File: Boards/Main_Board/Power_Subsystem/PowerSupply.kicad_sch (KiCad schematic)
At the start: 26 parts, among them IC4 LM2576HVS-5.0_NOPB, J10 KLDHCX-8-0202-A, U10 LM2576SX-3.3-NOPB

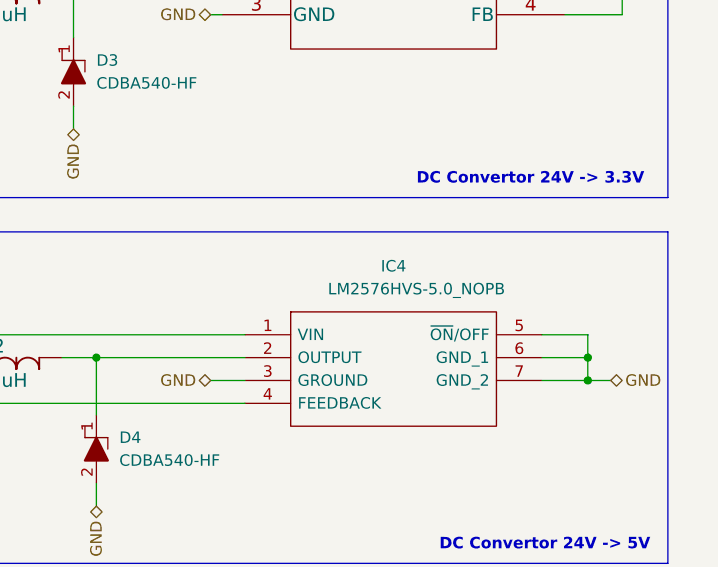
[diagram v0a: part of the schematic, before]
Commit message: Correct spacing on sensor board, refactor datasheets and project libraries
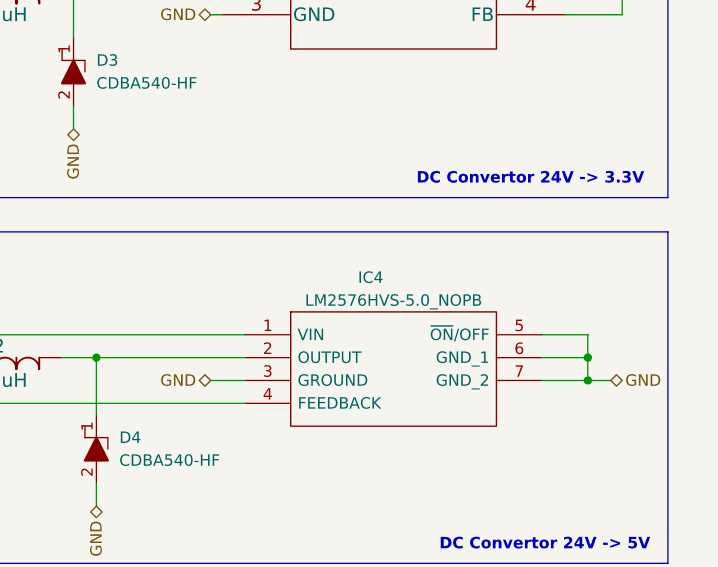
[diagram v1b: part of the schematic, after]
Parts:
- C25, C26: symbol CL10B104KB8NNC:CL10B104KB8NNNC -> CL10B104KB8NNNC:CL10B104KB8NNNC
- IC4: symbol LM25766HVS-5.0_NOPB:LM2576HVS-5.0_NOPB -> LM2576HVS-5.0_NOPB:LM2576HVS-5.0_NOPB
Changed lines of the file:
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@@
     (pin "2")
   )
-  (symbol (lib_id "CL10B104KB8NNC:CL10B104KB8NNNC") (at 123.19 148.59 90) (unit 1)
+  (symbol (lib_id "CL10B104KB8NNNC:CL10B104KB8NNNC") (at 123.19 148.59 90) (unit 1)
     (in_bom yes) (on_board yes)
     (property "Reference" "C26" (id 0) (at 118.11 146.05 90)
@@
     (pin "4")
   )
-  (symbol (lib_id "LM25766HVS-5.0_NOPB:LM2576HVS-5.0_NOPB") (at 184.15 133.35 0) (unit 1)
-    (in_bom yes) (on_board yes)
-    (property "Reference" "IC4" (id 0) (at 200.66 125.73 0))
-    (property "Value" "LM2576HVS-5.0_NOPB" (id 1) (at 203.2 128.27 0))
+  (symbol (lib_id "LM2576HVS-5.0_NOPB:LM2576HVS-5.0_NOPB") (at 184.15 133.35 0) (unit 1)
+    (in_bom yes) (on_board yes)
+    (property "Reference" "IC4" (id 0) (at 198.12 127 0))
+    (property "Value" "LM2576HVS-5.0_NOPB" (id 1) (at 200.66 129.54 0))
     (property "Footprint" "LM2576HVS50NOPB" (id 2) (at 218.44 130.81 0)
       (effects (font (size 1.27 1.27)) (justify left) hide)
@@
       (effects (font (size 1.27 1.27)) (justify left) hide)
     )
-    (property "Manufacturer's Part Number" "LM2576HVS-5.0/NOPB" (id 10) (at 184.15 133.35 0)
-      (effects (font (size 1.27 1.27)) hide)
+    (property "Manufacturer's Part Number" "LM2576HVS-5.0/NOPB" (id 10) (at 218.44 148.59 0)
+      (effects (font (size 1.27 1.27)) (justify left) hide)
     )
     (property "Digikey Part Number" "LM2576HVS-5.0/NOPB-ND" (id 11) (at 218.44 143.51 0)
@@
       (effects (font (size 1.27 1.27)) (justify left) hide)
     )
-    (property "Mouser Link" "https://www.mouser.com/ProductDetail/Texas-Instruments/LM2576HVS-5.0-NOPB?qs=X1J7HmVL2ZHJEgTkAH3ZCg%3D%3D" (id 8) (at 184.15 133.35 0)
+    (property "Mouser Link" "https://www.mouser.com/ProductDetail/Texas-Instruments/LM2576HVS-5.0-NOPB?qs=X1J7HmVL2ZHJEgTkAH3ZCg%3D%3D" (id 8) (at 196.85 123.19 0)
       (effects (font (size 1.27 1.27)) hide)
     )
@@
     (pin "")
   )
-  (symbol (lib_id "CL10B104KB8NNC:CL10B104KB8NNNC") (at 123.19 106.68 90) (unit 1)
+  (symbol (lib_id "CL10B104KB8NNNC:CL10B104KB8NNNC") (at 123.19 106.68 90) (unit 1)
     (in_bom yes) (on_board yes)
     (property "Reference" "C25" (id 0) (at 119.38 104.14 90)
@@
     (pin "2")
   )
-  (symbol (lib_id "860020573008:860020573008860020573008") (at 127 104.14 90) (mirror x) (unit 1)
+  (symbol (lib_name "860020573008860020573008_1") (lib_id "860020573008:860020573008860020573008") (at 127 104.14 90) (mirror x) (unit 1)
     (in_bom yes) (on_board yes)
     (property "Reference" "C27" (id 0) (at 135.89 101.6 90)
